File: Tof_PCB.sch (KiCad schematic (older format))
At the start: 62 parts, among them J1 Screw_Terminal_01x02, J2 Screw_Terminal_01x02, J3 Screw_Terminal_01x02, J4 Conn_02x03_Odd_Even, J5 Conn_01x04, J6 Conn_01x04, SW1 SW_Push, U1 ATmega328PB-MU, U2 DAC128S085, U3 LM4132BMF, Y1 Crystal_GND24

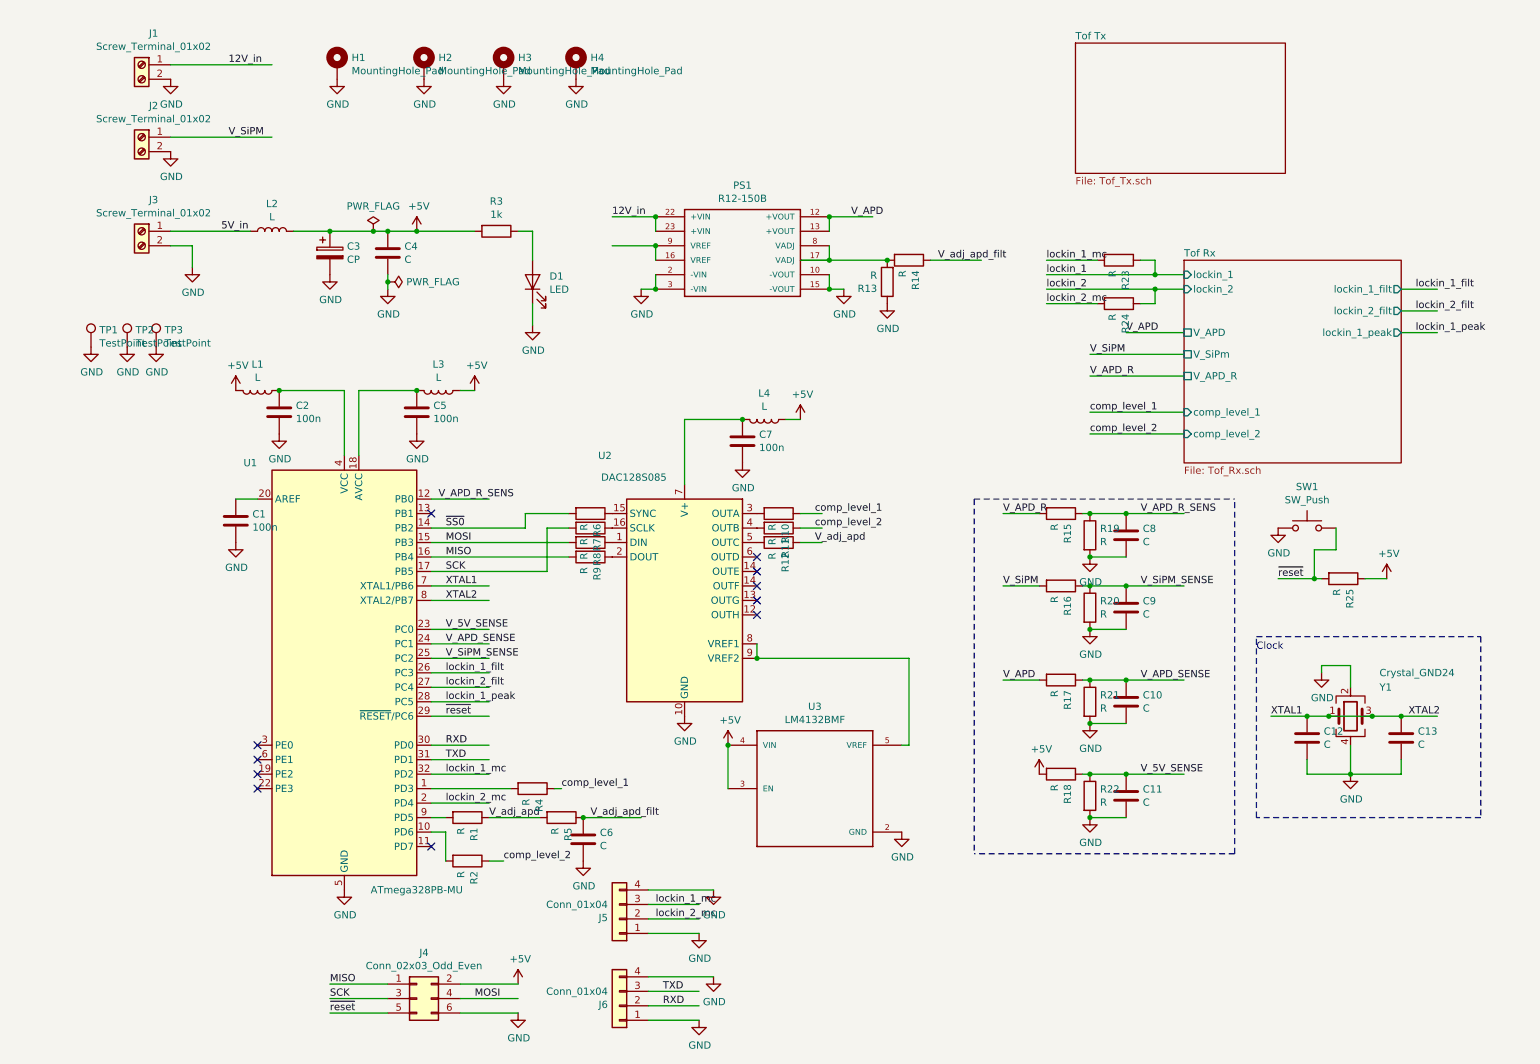
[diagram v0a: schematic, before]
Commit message: Added RLC values
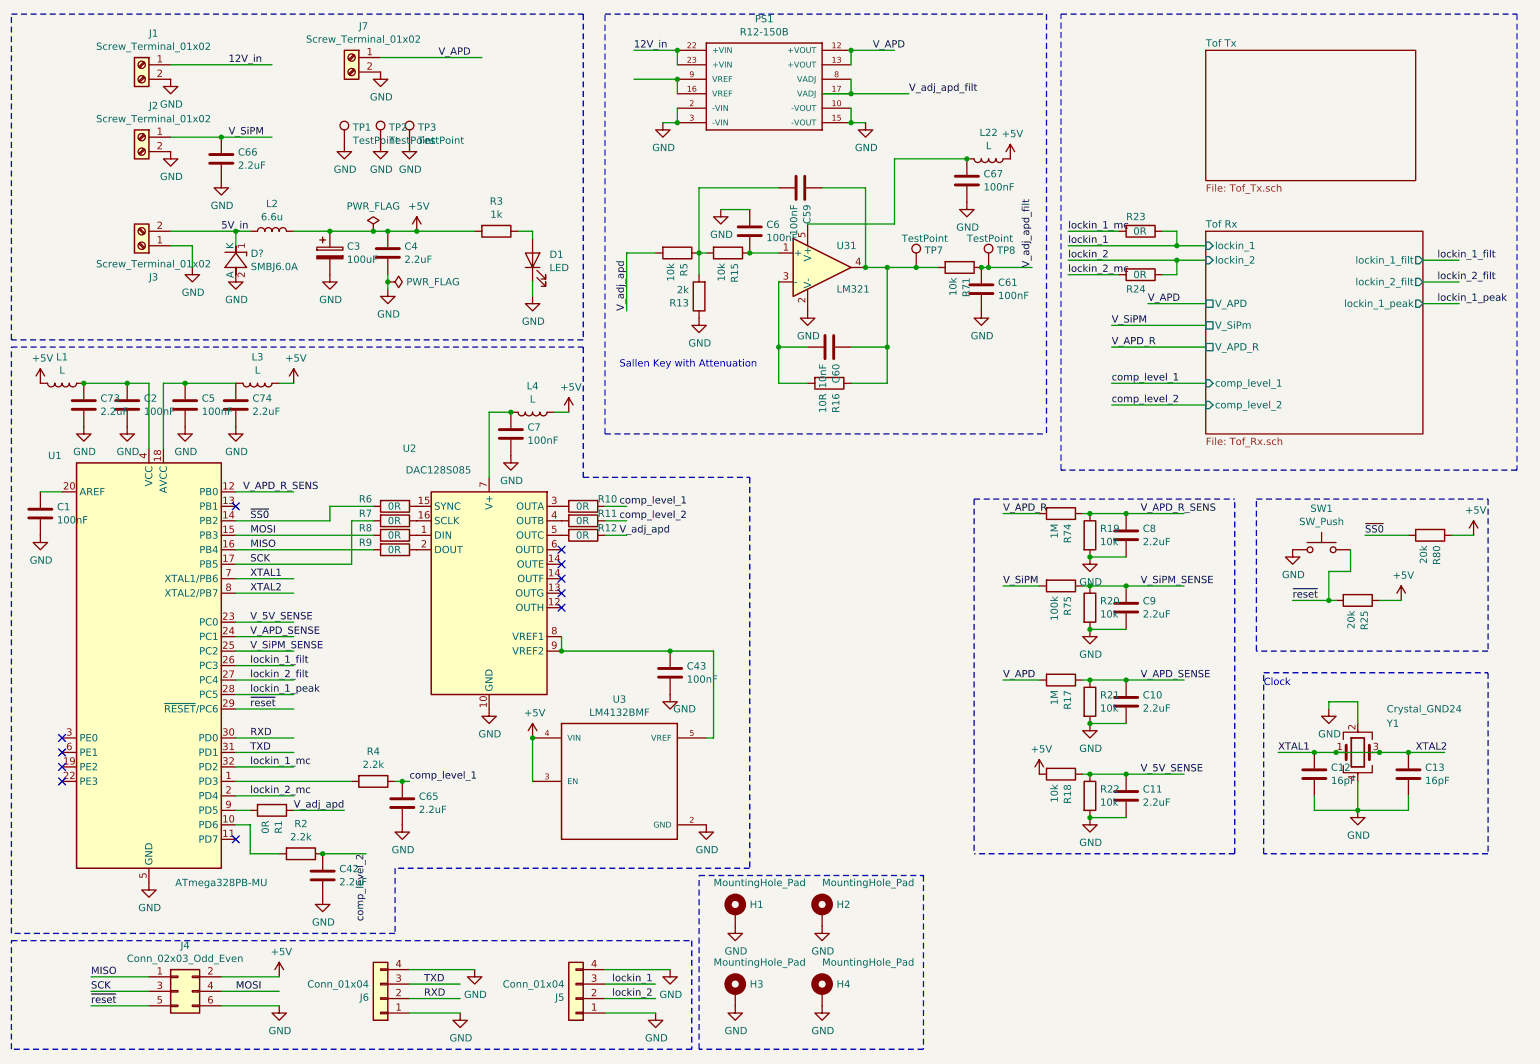
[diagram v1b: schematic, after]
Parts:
- removed R14: R, Resistor_SMD:R_0603_1608Metric, symbol Device:R
- added C42, C65, C66, C73, C74: 2.2uF, Capacitor_SMD:C_0603_1608Metric, symbol Device:C
- added C43, C59, C61, C67: 100nF, Capacitor_SMD:C_0603_1608Metric, symbol Device:C
- added C60: 10nF, Capacitor_SMD:C_0603_1608Metric, symbol Device:C
- added D?: SMBJ6.0A, OLIMEX_Diodes-FP:DO214AA, symbol OLIMEX_Diodes:SMBJ6.0A
- added J7: Screw_Terminal_01x02, IODA_Lib:ScrewTerminal_1x02_P2.54mm_Vertical, symbol Connector:Screw_Terminal_01x02
- added L22: L, Inductor_SMD:L_0603_1608Metric, symbol Device:L
- added R71: 10k, Resistor_SMD:R_0603_1608Metric, symbol Device:R
- added R74: 1M, Resistor_SMD:R_0603_1608Metric, symbol Device:R
- added R75: 100k, Resistor_SMD:R_0603_1608Metric, symbol Device:R
- added R80: 20k, Resistor_SMD:R_0603_1608Metric, symbol Device:R
- added TP7, TP8: TestPoint, Connector_PinHeader_1.00mm:PinHeader_1x01_P1.00mm_Vertical, symbol Connector:TestPoint
- added U31: LM321, Package_TO_SOT_SMD:SOT-23-5, symbol Amplifier_Operational:LM321
- C1, C2, C5, C7: value 100n -> 100nF
- C10, C11, C4, C8, C9: value C -> 2.2uF
- C12, C13: value C -> 16pF
- C3: value CP -> 100uF
- C6: value C -> 100nF
- L2: value L -> 6.6u
- R1, R10, R11, R12, R23, R24, R6, R7, R8, R9: value R -> 0R
- R13: value R -> 2k
- R15, R18, R19, R20, R21, R22, R5: value R -> 10k
- R16: value R -> 10R
- R17: value R -> 1M
- R2, R4: value R -> 2.2k
- R25: value R -> 20k
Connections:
- wire segments 146 -> 181
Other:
- note added: "Sallen Key with Attenuation"
- moved on the sheet: C1, C12, C13, C2, C5, C7, D1, H1, H2, H3, H4, J4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

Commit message: Added more digikey numbers in BOM
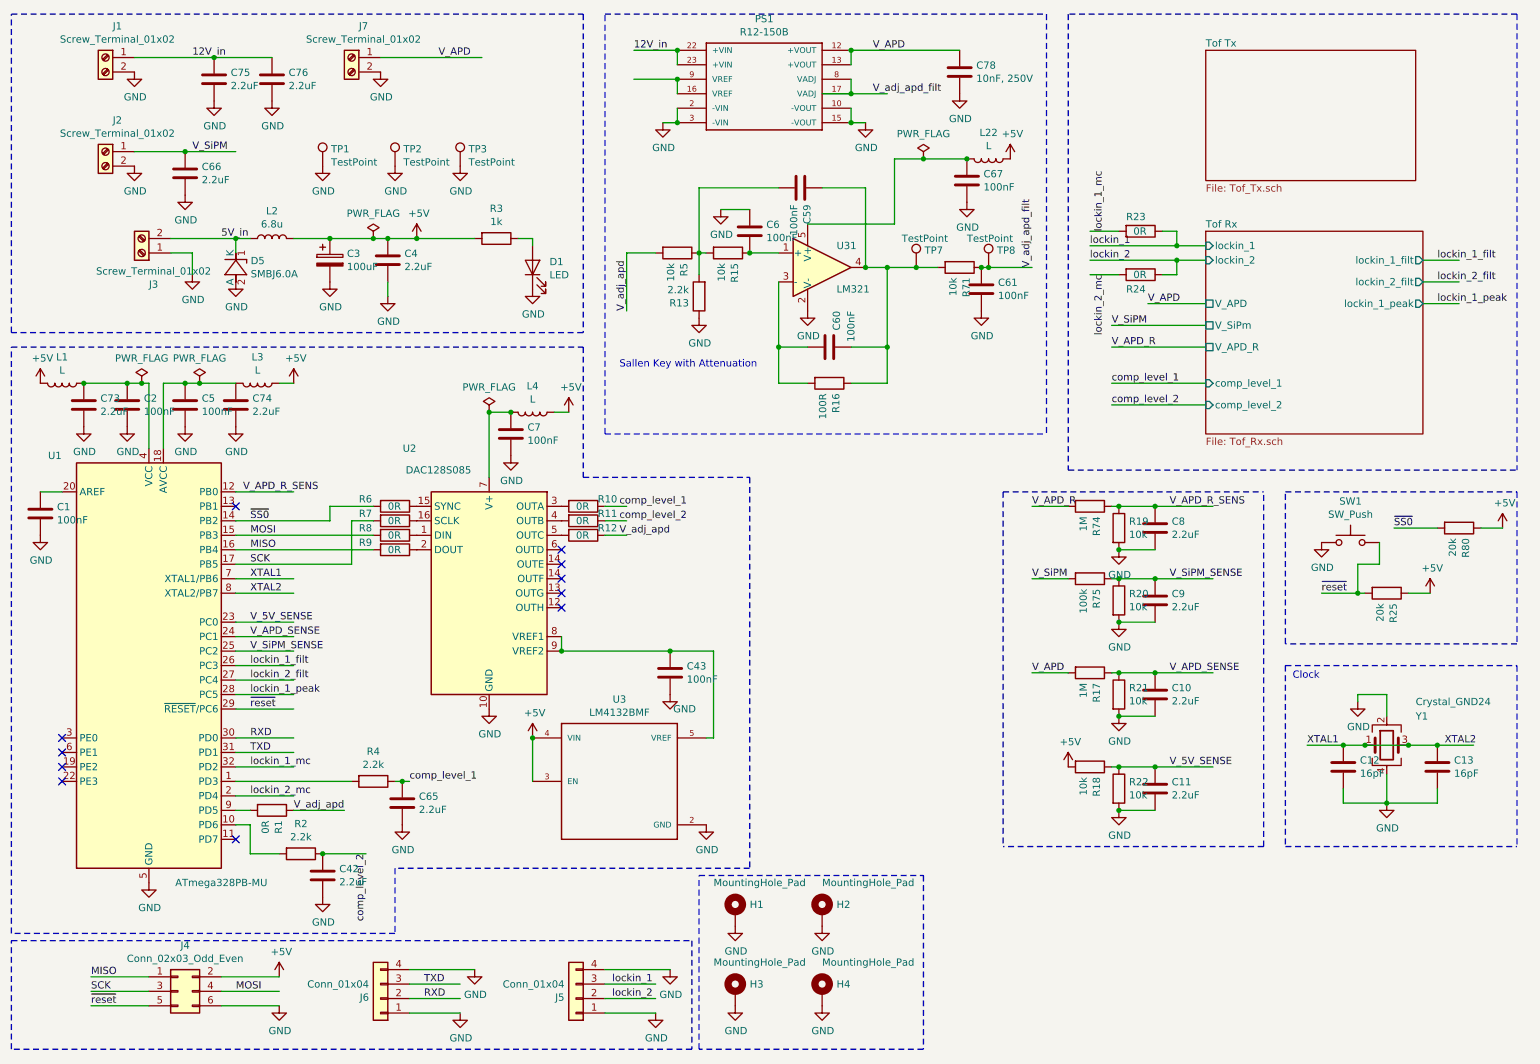
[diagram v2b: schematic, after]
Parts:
- added C75, C76: 2.2uF, Capacitor_SMD:C_0603_1608Metric, symbol Device:C
- added C78: 10nF, 250V, Capacitor_SMD:C_0603_1608Metric, symbol Device:C
- C3: Digi-Key_PN (none) -> PCE5024CT-ND
- C60: value 10nF -> 100nF
- D1: Digi-Key_PN (none) -> 160-1423-1-ND
- D5: renamed from D?; footprint OLIMEX_Diodes-FP:DO214AA -> OLIMEX_Diodes-FP:DO214AA_1(K)-2(A); Digi-Key_PN (none) -> SMBJ6.0ABCT-ND
- J1, J2, J3, J7: Digi-Key_PN (none) -> A98333-ND
- J5, J6: Digi-Key_PN (none) -> WM7622CT-ND
- L1, L22, L3, L4: Digi-Key_PN (none) -> 490-5216-1-ND
- L2: value 6.6u -> 6.8u; Digi-Key_PN (none) -> 811-1180-1-ND
- PS1: Digi-Key_PN (none) -> 945-2053-5-ND
- R13: value 2k -> 2.2k
- R16: value 10R -> 100R
- SW1: Digi-Key_PN (none) -> CKN9112TR-ND
- TP1, TP2, TP3, TP7, TP8: Digi-Key_PN (none) -> 732-5314-ND
- U1: Digi-Key_PN (none) -> ATMEGA328PB-MURCT-ND
- U2: Digi-Key_PN (none) -> DAC128S085CIMT/NOPB
- U3: Digi-Key_PN (none) -> LM4132BMF-4.1/NOPBCT-ND
- U31: Digi-Key_PN (none) -> LM321MFX/NOPBCT-ND
- Y1: Digi-Key_PN (none) -> SER4068CT-ND
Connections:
- wire segments 181 -> 183
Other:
- moved on the sheet: C10, C11, C12, C13, C3, C4, C66, C8, C9, D1, D5, J1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

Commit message: solved drc errors
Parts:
- added R65, R81, R82, R83: 0R, Resistor_SMD:R_0603_1608Metric, symbol Device:R
- D1: footprint LEDs:LED_0805_HandSoldering -> LEDs:LED_0805
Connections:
- wire segments 183 -> 182
- no-connect marks 11 -> 13
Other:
- moved on the sheet: H1, H2, H3, H4
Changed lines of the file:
@@
 F 0 "D1" V 4189 2233 50  0000 R CNN
 F 1 "LED" V 4098 2233 50  0000 R CNN
-F 2 "LEDs:LED_0805_HandSoldering" H 4150 2350 50  0001 C CNN
+F 2 "LEDs:LED_0805" H 4150 2350 50  0001 C CNN
 F 3 "~" H 4150 2350 50  0001 C CNN
 F 4 "160-1423-1-ND" H 4150 2350 50  0001 C CNN "Digi-Key_PN"
@@
 Wire Wire Line
 	4850 850  5150 850
-Wire Wire Line
-	5150 1150 5150 1050
-Wire Wire Line
-	5150 1050 4850 1050
-Connection ~ 5150 1050
 Wire Wire Line
 	6350 1350 6350 1250
@@
 F 1 "Crystal_GND24" H 10250 5950 50  0000 L CNN
 F 2 "Crystal:Crystal_SMD_2520-4Pin_2.5x2.0mm" H 10050 5650 50  0001 C CNN
-F 3 "https://support.epson.biz/td/api/doc_check.php?dl=brief_FA-20H&lang=en" H 10050 5650 50  0001 C CNN
+F 3 "~" H 10050 5650 50  0001 C CNN
 F 4 "SER4068CT-ND" H 10050 5650 50  0001 C CNN "Digi-Key_PN"
 	1    10050 5650
@@
 Wire Wire Line
 	9750 5650 9900 5650
-Connection ~ 9900 5650
-Wire Wire Line
-	9900 5650 10200 5650
-Connection ~ 10200 5650
-Wire Wire Line
-	10200 5650 10400 5650
+Wire Wire Line
+	10200 5650 10250 5650
 Wire Wire Line
 	10400 5650 10650 5650
@@
 L Mechanical:MountingHole_Pad H1
 U 1 1 5DDB4814
-P 5550 6800
-F 0 "H1" H 5650 6849 50  0000 L CNN
-F 1 "MountingHole_Pad" H 5400 7000 50  0000 L CNN
-F 2 "MountingHole:MountingHole_2.2mm_M2" H 5550 6800 50  0001 C CNN
-F 3 "~" H 5550 6800 50  0001 C CNN
-	1    5550 6800
+P 6050 4350
+F 0 "H1" H 6150 4399 50  0000 L CNN
+F 1 "MountingHole_Pad" H 5900 4650 50  0000 L CNN
+F 2 "MountingHole:MountingHole_2.2mm_M2" H 6050 4350 50  0001 C CNN
+F 3 "~" H 6050 4350 50  0001 C CNN
+	1    6050 4350
 	1    0    0    -1
 $EndComp
@@
 L power:GND #PWR0141
 U 1 1 5DDB4D6B
-P 5550 6900
-F 0 "#PWR0141" H 5550 6650 50  0001 C CNN
-F 1 "GND" H 5555 6727 50  0000 C CNN
-F 2 "" H 5550 6900 50  0001 C CNN
-F 3 "" H 5550 6900 50  0001 C CNN
-	1    5550 6900
-	1    0    0    -1
-$EndComp
-$Comp
-L power:GND #PWR0142
-U 1 1 5DDBE3F6
-P 6150 6900
-F 0 "#PWR0142" H 6150 6650 50  0001 C CNN
-F 1 "GND" H 6155 6727 50  0000 C CNN
-F 2 "" H 6150 6900 50  0001 C CNN
-F 3 "" H 6150 6900 50  0001 C CNN
-	1    6150 6900
+P 6050 4750
+F 0 "#PWR0141" H 6050 4500 50  0001 C CNN
+F 1 "GND" H 6055 4577 50  0000 C CNN
+F 2 "" H 6050 4750 50  0001 C CNN
+F 3 "" H 6050 4750 50  0001 C CNN
+	1    6050 4750
 	1    0    0    -1
 $EndComp
@@
 L power:GND #PWR0143
 U 1 1 5DDC6C1A
-P 5550 7450
-F 0 "#PWR0143" H 5550 7200 50  0001 C CNN
-F 1 "GND" H 5555 7277 50  0000 C CNN
-F 2 "" H 5550 7450 50  0001 C CNN
-F 3 "" H 5550 7450 50  0001 C CNN
-	1    5550 7450
+P 6050 5850
+F 0 "#PWR0143" H 6050 5600 50  0001 C CNN
+F 1 "GND" H 6055 5677 50  0000 C CNN
+F 2 "" H 6050 5850 50  0001 C CNN
+F 3 "" H 6050 5850 50  0001 C CNN
+	1    6050 5850
 	1    0    0    -1
 $EndComp
@@
 L power:GND #PWR0144
 U 1 1 5DDCF524
-P 6150 7450
-F 0 "#PWR0144" H 6150 7200 50  0001 C CNN
-F 1 "GND" H 6155 7277 50  0000 C CNN
-F 2 "" H 6150 7450 50  0001 C CNN
-F 3 "" H 6150 7450 50  0001 C CNN
-	1    6150 7450
-	1    0    0    -1
-$EndComp
-$Comp
-L Mechanical:MountingHole_Pad H2
-U 1 1 5DDE02A3
-P 6150 6800
-F 0 "H2" H 6250 6849 50  0000 L CNN
-F 1 "MountingHole_Pad" H 6150 7000 50  0000 L CNN
-F 2 "MountingHole:MountingHole_2.2mm_M2" H 6150 6800 50  0001 C CNN
-F 3 "~" H 6150 6800 50  0001 C CNN
-	1    6150 6800
+P 6600 5850
+F 0 "#PWR0144" H 6600 5600 50  0001 C CNN
+F 1 "GND" H 6605 5677 50  0000 C CNN
+F 2 "" H 6600 5850 50  0001 C CNN
+F 3 "" H 6600 5850 50  0001 C CNN
+	1    6600 5850
 	1    0    0    -1
 $EndComp
@@
 L Mechanical:MountingHole_Pad H3
 U 1 1 5DDE0575
-P 5550 7350
-F 0 "H3" H 5650 7399 50  0000 L CNN
-F 1 "MountingHole_Pad" H 5400 7550 50  0000 L CNN
-F 2 "MountingHole:MountingHole_2.2mm_M2" H 5550 7350 50  0001 C CNN
-F 3 "~" H 5550 7350 50  0001 C CNN
-	1    5550 7350
+P 6050 5450
+F 0 "H3" H 6150 5499 50  0000 L CNN
+F 1 "MountingHole_Pad" H 5900 5750 50  0000 L CNN
+F 2 "MountingHole:MountingHole_2.2mm_M2" H 6050 5450 50  0001 C CNN
+F 3 "~" H 6050 5450 50  0001 C CNN
+	1    6050 5450
 	1    0    0    -1
 $EndComp
@@
 L Mechanical:MountingHole_Pad H4
 U 1 1 5DDE0753
-P 6150 7350
-F 0 "H4" H 6250 7399 50  0000 L CNN
-F 1 "MountingHole_Pad" H 6150 7550 50  0000 L CNN
-F 2 "MountingHole:MountingHole_2.2mm_M2" H 6150 7350 50  0001 C CNN
-F 3 "~" H 6150 7350 50  0001 C CNN
-	1    6150 7350
+P 6600 5450
+F 0 "H4" H 6700 5499 50  0000 L CNN
+F 1 "MountingHole_Pad" H 6500 5650 50  0000 L CNN
+F 2 "MountingHole:MountingHole_2.2mm_M2" H 6600 5450 50  0001 C CNN
+F 3 "~" H 6600 5450 50  0001 C CNN
+	1    6600 5450
 	1    0    0    -1
 $EndComp
@@
 	550  7750 550  7000
 Wire Notes Line
-	5300 6550 6850 6550
-Wire Notes Line
-	6850 6550 6850 7750
-Wire Notes Line
 	6850 7750 5300 7750
-Wire Notes Line
-	5300 7750 5300 6550
 $Comp
 L Device:C C73
@@
 Connection ~ 1950 900
 Wire Wire Line
-	1950 900  2350 900
+	1950 900  2200 900
 Wire Notes Line
 	4500 600  4500 2800
@@
 Wire Wire Line
 	6850 1600 6650 1600
+NoConn ~ 5150 1050
+NoConn ~ 5150 1150
+$Comp
+L Mechanical:MountingHole_Pad H2
+U 1 1 5DDE02A3
+P 6600 4350
+F 0 "H2" H 6700 4399 50  0000 L CNN
+F 1 "MountingHole_Pad" H 6500 4550 50  0000 L CNN
+F 2 "MountingHole:MountingHole_2.2mm_M2" H 6600 4350 50  0001 C CNN
+F 3 "~" H 6600 4350 50  0001 C CNN
+	1    6600 4350
+	1    0    0    -1
+$EndComp
+$Comp
+L power:GND #PWR0142
+U 1 1 5DDBE3F6
+P 6600 4750
+F 0 "#PWR0142" H 6600 4500 50  0001 C CNN
+F 1 "GND" H 6605 4577 50  0000 C CNN
+F 2 "" H 6600 4750 50  0001 C CNN
+F 3 "" H 6600 4750 50  0001 C CNN
+	1    6600 4750
+	1    0    0    -1
+$EndComp
+$Comp
+L Device:R R?
+U 1 1 5E312F59
+P 6600 4600
+AR Path="/5DD4CF74/5E312F59" Ref="R?"  Part="1"
+AR Path="/5E312F59" Ref="R82"  Part="1"
+F 0 "R82" V 6500 4550 50  0000 L CNN
+F 1 "0R" V 6600 4550 50  0000 L CNN
+F 2 "Resistor_SMD:R_0603_1608Metric" V 6530 4600 50  0001 C CNN
+F 3 "~" H 6600 4600 50  0001 C CNN
+	1    6600 4600
+	1    0    0    -1
+$EndComp
+$Comp
+L Device:R R?
+U 1 1 5E36A4B4
+P 6050 4600
+AR Path="/5DD4CF74/5E36A4B4" Ref="R?"  Part="1"
+AR Path="/5E36A4B4" Ref="R65"  Part="1"
+F 0 "R65" V 5950 4550 50  0000 L CNN
+F 1 "0R" V 6050 4550 50  0000 L CNN
+F 2 "Resistor_SMD:R_0603_1608Metric" V 5980 4600 50  0001 C CNN
+F 3 "~" H 6050 4600 50  0001 C CNN
+	1    6050 4600
+	1    0    0    -1
+$EndComp
+$Comp
+L Device:R R?
+U 1 1 5E3865AD
+P 6050 5700
+AR Path="/5DD4CF74/5E3865AD" Ref="R?"  Part="1"
+AR Path="/5E3865AD" Ref="R81"  Part="1"
+F 0 "R81" V 5950 5650 50  0000 L CNN
+F 1 "0R" V 6050 5650 50  0000 L CNN
+F 2 "Resistor_SMD:R_0603_1608Metric" V 5980 5700 50  0001 C CNN
+F 3 "~" H 6050 5700 50  0001 C CNN
+	1    6050 5700
+	1    0    0    -1
+$EndComp
+$Comp
+L Device:R R?
+U 1 1 5E394597
+P 6600 5700
+AR Path="/5DD4CF74/5E394597" Ref="R?"  Part="1"
+AR Path="/5E394597" Ref="R83"  Part="1"
+F 0 "R83" V 6500 5650 50  0000 L CNN
+F 1 "0R" V 6600 5650 50  0000 L CNN
+F 2 "Resistor_SMD:R_0603_1608Metric" V 6530 5700 50  0001 C CNN
+F 3 "~" H 6600 5700 50  0001 C CNN
+	1    6600 5700
+	1    0    0    -1
+$EndComp
+Wire Notes Line
+	5800 3900 7250 3900
+Wire Notes Line
+	7250 3900 7250 6350
+Wire Notes Line
+	5800 6350 5800 3900
+Wire Notes Line
+	5800 6350 7250 6350
+$Comp
+L power:PWR_FLAG #FLG0112
+U 1 1 5E493E9C
+P 2200 900
+F 0 "#FLG0112" H 2200 975 50  0001 C CNN
+F 1 "PWR_FLAG" H 2200 1073 50  0000 C CNN
+F 2 "" H 2200 900 50  0001 C CNN
+F 3 "~" H 2200 900 50  0001 C CNN
+	1    2200 900
+	1    0    0    -1
+$EndComp
+Connection ~ 2200 900
+Wire Wire Line
+	2200 900  2350 900
+$Comp
+L power:PWR_FLAG #FLG0113
+U 1 1 5E4A0FE7
+P 4200 1000
+F 0 "#FLG0113" H 4200 1075 50  0001 C CNN
+F 1 "PWR_FLAG" H 4200 1173 50  0000 C CNN
+F 2 "" H 4200 1000 50  0001 C CNN
+F 3 "~" H 4200 1000 50  0001 C CNN
+	1    4200 1000
+	1    0    0    -1
+$EndComp
+$Comp
+L power:GND #PWR0175
+U 1 1 5E4A1F1C
+P 4200 1000
+F 0 "#PWR0175" H 4200 750 50  0001 C CNN
+F 1 "GND" H 4205 827 50  0000 C CNN
+F 2 "" H 4200 1000 50  0001 C CNN
+F 3 "" H 4200 1000 50  0001 C CNN
+	1    4200 1000
+	1    0    0    -1
+$EndComp
+Connection ~ 10250 5650
+Wire Wire Line
+	10250 5650 10400 5650
 $EndSCHEMATC

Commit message: bugfixes
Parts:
- added C80: 2.2uF, Capacitor_SMD:C_0603_1608Metric, symbol Device:C
- added FID1, FID2, FID3: Fiducial, MF_Aesthetics:MF_Aesthetics-FIDUCIAL_100MIL, symbol Mechanical:Fiducial
- added R85: 50R, Resistor_SMD:R_0603_1608Metric, symbol Device:R
- added R92, R93: 10k, Resistor_SMD:R_0603_1608Metric, symbol Device:R
- added U33: UMCC_50Ohm, IODA_Lib:Molex_734120114_UMC_RF_CONN_Vertical, symbol ioda:UMCC_50Ohm
- C1, C2, C43, C5, C59, C6, C60, C61, C67, C7: Digi-Key_PN (none) -> 490-3285-1-ND
- C10, C11, C4, C42, C65, C66, C73, C74, C75, C76, C8, C9: Digi-Key_PN (none) -> 490-12740-1-ND
- C12, C13: Digi-Key_PN (none) -> 399-7863-1-ND
- C78: Digi-Key_PN (none) -> 732-12168-1-ND
- J4: Digi-Key_PN (none) -> 609-3210-ND
- L1, L22, L3, L4: value L -> bead
- PS1, SW1, U2, U3: Configuration (none) -> do not mount
- R1, R23, R24, R6, R7, R8, R9: Digi-Key_PN (none) -> RMCF0603ZT0R00CT-ND
- R10, R11, R12, R65, R81, R82, R83: Configuration (none) -> do not mount; Digi-Key_PN (none) -> RMCF0603ZT0R00CT-ND
- R13, R2, R4: Digi-Key_PN (none) -> RMCF0603FT2K20CT-ND
- R15, R18, R19, R20, R21, R22, R5, R71: Digi-Key_PN (none) -> P10.0KHCT-ND
- R16: Digi-Key_PN (none) -> RMCF0603FT100R
- R17, R74: Digi-Key_PN (none) -> 311-1.00MHRCT-ND
- R25, R80: value 20k -> 10k; Digi-Key_PN (none) -> P10.0KHCT-ND
- R3: value 1k -> 2.2k; Digi-Key_PN (none) -> RMCF0603FT2K20CT-ND
- R75: Digi-Key_PN (none) -> RMCF0603FT110K
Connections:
- net labels added: start_mc, stop_mc
- wire segments 182 -> 187
- no-connect marks 13 -> 11
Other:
- moved on the sheet: J4, J5, J6
